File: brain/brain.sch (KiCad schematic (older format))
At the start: 0 parts

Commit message: footprint assignation
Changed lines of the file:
@@
 LIBS:contrib
 LIBS:valves
-LIBS:stm32
 LIBS:espitall
 LIBS:brain-cache
@@
 F11 "SLA_ALERT3_3v3" I R 2200 4700 60
 F12 "SLA_ALERT2_3v3" I R 2200 4600 60
+F13 "SLA_TX_3v3" I R 2200 3500 60
+F14 "SLA_RX_3v3" O R 2200 3600 60
 $EndSheet
 $Sheet
@@
 F1 "supply.sch" 60
 $EndSheet
+Wire Wire Line
+	2200 3600 4000 3600
+Wire Wire Line
+	4000 3500 2200 3500
 $EndSCHEMATC

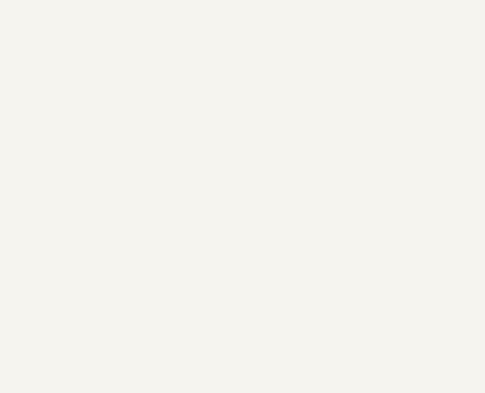
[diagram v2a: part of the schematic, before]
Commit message: add mounting holes
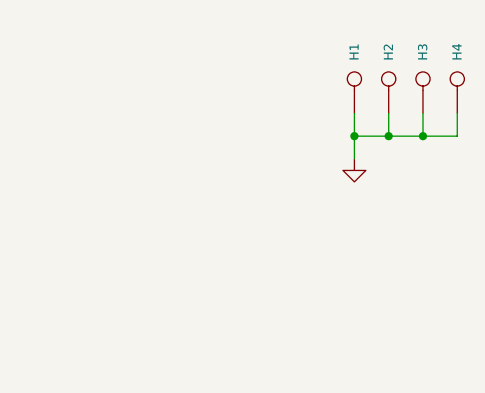
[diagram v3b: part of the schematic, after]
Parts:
- added H1, H2, H3, H4: CONN_1, Mounting_Holes:MountingHole_3-5mm, symbol CONN_1
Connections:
- new net GND: H1.1, H2.1, H3.1, H4.1
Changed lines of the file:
@@
 Wire Wire Line
 	4000 3500 2200 3500
+$Comp
+L CONN_1 H1
+U 1 1 5566D8A1
+P 10250 750
+F 0 "H1" H 10330 750 40  0000 L CNN
+F 1 "CONN_1" H 10250 805 30  0001 C CNN
+F 2 "Mounting_Holes:MountingHole_3-5mm" H 10250 750 60  0001 C CNN
+F 3 "" H 10250 750 60  0000 C CNN
+	1    10250 750
+	0    -1   -1   0
+$EndComp
+$Comp
+L CONN_1 H2
+U 1 1 5566FA8C
+P 10400 750
+F 0 "H2" H 10480 750 40  0000 L CNN
+F 1 "CONN_1" H 10400 805 30  0001 C CNN
+F 2 "Mounting_Holes:MountingHole_3-5mm" H 10400 750 60  0001 C CNN
+F 3 "" H 10400 750 60  0000 C CNN
+	1    10400 750
+	0    -1   -1   0
+$EndComp
+$Comp
+L CONN_1 H3
+U 1 1 5566FC24
+P 10550 750
+F 0 "H3" H 10630 750 40  0000 L CNN
+F 1 "CONN_1" H 10550 805 30  0001 C CNN
+F 2 "Mounting_Holes:MountingHole_3-5mm" H 10550 750 60  0001 C CNN
+F 3 "" H 10550 750 60  0000 C CNN
+	1    10550 750
+	0    -1   -1   0
+$EndComp
+$Comp
+L CONN_1 H4
+U 1 1 5566FDBE
+P 10700 750
+F 0 "H4" H 10780 750 40  0000 L CNN
+F 1 "CONN_1" H 10700 805 30  0001 C CNN
+F 2 "Mounting_Holes:MountingHole_3-5mm" H 10700 750 60  0001 C CNN
+F 3 "" H 10700 750 60  0000 C CNN
+	1    10700 750
+	0    -1   -1   0
+$EndComp
+$Comp
+L GND #PWR01
+U 1 1 55670260
+P 10250 1100
+F 0 "#PWR01" H 10250 1100 30  0001 C CNN
+F 1 "GND" H 10250 1030 30  0001 C CNN
+F 2 "" H 10250 1100 60  0000 C CNN
+F 3 "" H 10250 1100 60  0000 C CNN
+	1    10250 1100
+	1    0    0    -1
+$EndComp
+Wire Wire Line
+	10250 900  10250 1100
+Wire Wire Line
+	10250 1000 10700 1000
+Wire Wire Line
+	10700 1000 10700 900
+Connection ~ 10250 1000
+Wire Wire Line
+	10550 900  10550 1000
+Connection ~ 10550 1000
+Wire Wire Line
+	10400 900  10400 1000
+Connection ~ 10400 1000
 $EndSCHEMATC

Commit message: Brain 2018 layout
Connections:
- removed net GND: H1.1, H2.1, H3.1, H4.1
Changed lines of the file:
@@
 EESchema Schematic File Version 2
+LIBS:brain-rescue
 LIBS:power
 LIBS:device
@@
 LIBS:memory
 LIBS:xilinx
-LIBS:special
 LIBS:microcontrollers
 LIBS:dsp
@@
 $Descr A4 11693 8268
 encoding utf-8
-Sheet 1 8
+Sheet 1 9
 Title "Brain"
-Date ""
-Rev "2016"
-Comp "espitall"
-Comment1 "Board for eurobot 2016 (French edition)"
+Date "2017-05-28"
+Rev "2018"
+Comp "Cocobot"
+Comment1 "Board for eurobot 2018 (French edition)"
 Comment2 ""
 Comment3 ""
@@
 F11 "MOTL_PWM_3v3" I L 7200 5150 60
 F12 "MOTR_PWM_3v3" I L 7200 5350 60
-F13 "AX12_TX_3v3" I R 8600 4950 60
-F14 "AX12_RX_3v3" O R 8600 5050 60
-F15 "AX12_TX_5v" O R 8600 5150 60
-F16 "AX12_RX_5v" I R 8600 5250 60
-$EndSheet
-$Sheet
-S 7200 3800 1400 700
+$EndSheet
+$Sheet
+S 7200 3700 1350 300
 U 5563C415
 F0 "Servo" 60
 F1 "Servo.sch" 60
-F2 "I2C_SCL_3v3" I L 7200 4100 60
-F3 "I2C_SDA_3v3" B L 7200 4200 60
-F4 "AX12_TX_5v" I R 8600 4200 60
-F5 "AX12_RX_5v" O R 8600 4100 60
+F2 "I2C_SCL_3v3" I L 7200 3800 60
+F3 "I2C_SDA_3v3" B L 7200 3900 60
 $EndSheet
 $Sheet
@@
 F22 "MOTL_PWM_3v3" O R 6400 5150 60
 F23 "MOTR_PWM_3v3" O R 6400 5350 60
-F24 "I2C_SCL_3v3" O R 6400 4100 60
-F25 "I2C_SDA_3v3" B R 6400 4200 60
+F24 "I2C_SCL_3v3" O R 6400 3800 60
+F25 "I2C_SDA_3v3" B R 6400 3900 60
 F26 "IR_CH0_0_3v3" I L 4000 6350 60
 F27 "IR_CH1_0_3v3" I L 4000 6450 60
@@
 F35 "GPIO_SHIFT_OE_3v3" O R 6400 3000 60
 F36 "GPIO_SHIFT_STCP_3v3" O R 6400 2900 60
-F37 "AX12_TX_3v3" O R 6400 4700 60
-F38 "AX12_RX_3v3" I R 6400 4600 60
-F39 "US_CH0_E_3v3" I L 4000 5500 60
-F40 "US_CH1_E_3v3" I L 4000 5700 60
-F41 "US_CH3_E_3v3" I L 4000 6100 60
-F42 "US_CH2_E_3v3" I L 4000 5900 60
-F43 "US_CH1_T_3v3" O L 4000 5600 60
-F44 "US_CH0_T_3v3" O L 4000 5400 60
-F45 "US_CH3_T_3v3" O L 4000 6000 60
-F46 "US_CH2_T_3v3" O L 4000 5800 60
-F47 "GPIO0_3v3" B R 6400 1350 60
-F48 "GPIO1_3v3" B R 6400 1450 60
-F49 "GPIO2_3v3" B R 6400 1550 60
-F50 "GPIO3_3v3" B R 6400 1650 60
-F51 "GPIO4_3v3" B R 6400 1750 60
-F52 "GPIO5_3v3" B R 6400 1850 60
-F53 "GPIO6_3v3" B R 6400 1950 60
-F54 "GPIO7_3v3" B R 6400 2050 60
-F55 "GPIO8_3v3" B R 6400 2150 60
-F56 "GPIO9_3v3" B R 6400 2250 60
-F57 "GPIO10_3v3" B R 6400 2350 60
-F58 "GPIO11_3v3" B R 6400 2450 60
-F59 "STARTER_3v3" I R 6400 2550 60
-F60 "COLOR_3v3" I R 6400 2650 60
-F61 "SLA_TX_3v3" O L 4000 3500 60
-F62 "SLA_RX_3v3" I L 4000 3600 60
+F37 "US_CH0_E_3v3" I L 4000 5500 60
+F38 "US_CH1_E_3v3" I L 4000 5700 60
+F39 "US_CH3_E_3v3" I L 4000 6100 60
+F40 "US_CH2_E_3v3" I L 4000 5900 60
+F41 "US_CH1_T_3v3" O L 4000 5600 60
+F42 "US_CH0_T_3v3" O L 4000 5400 60
+F43 "US_CH3_T_3v3" O L 4000 6000 60
+F44 "US_CH2_T_3v3" O L 4000 5800 60
+F45 "GPIO0_3v3" B R 6400 1350 60
+F46 "GPIO1_3v3" B R 6400 1450 60
+F47 "GPIO2_3v3" B R 6400 1550 60
+F48 "GPIO3_3v3" B R 6400 1650 60
+F49 "GPIO4_3v3" B R 6400 1750 60
+F50 "GPIO5_3v3" B R 6400 1850 60
+F51 "GPIO6_3v3" B R 6400 1950 60
+F52 "GPIO7_3v3" B R 6400 2050 60
+F53 "GPIO8_3v3" B R 6400 2150 60
+F54 "GPIO9_3v3" B R 6400 2250 60
+F55 "GPIO10_3v3" B R 6400 2350 60
+F56 "GPIO11_3v3" B R 6400 2450 60
+F57 "STARTER_3v3" I R 6400 2550 60
+F58 "COLOR_3v3" I R 6400 2650 60
+F59 "SLA_TX_3v3" O L 4000 3500 60
+F60 "SLA_RX_3v3" I L 4000 3600 60
+F61 "DCM_PWM_0_3v3" O R 6400 4350 60
+F62 "DCM_PWM_1_3v3" O R 6400 4450 60
+F63 "DCM_DIR_0_3v3" O R 6400 4250 60
+F64 "DCM_DIR_1_3v3" O R 6400 4150 60
 $EndSheet
 Wire Wire Line
@@
 	6400 5050 7200 5050
 Wire Wire Line
-	7200 4950 6400 4950
+	6400 4950 7200 4950
 Wire Wire Line
 	7200 3300 3700 3300
@@
 	6400 1350 7200 1350
 Wire Wire Line
-	6400 4600 8900 4600
-Wire Wire Line
-	8900 4600 8900 5050
-Wire Wire Line
-	8900 5050 8600 5050
-Wire Wire Line
-	6400 4700 8800 4700
-Wire Wire Line
-	8800 4700 8800 4950
-Wire Wire Line
-	8800 4950 8600 4950
-Wire Wire Line
-	6400 4200 7200 4200
-Wire Wire Line
-	7200 4100 6400 4100
-Wire Wire Line
-	8600 5150 9000 5150
-Wire Wire Line
-	9000 5150 9000 4200
-Wire Wire Line
-	9000 4200 8600 4200
-Wire Wire Line
-	8600 5250 9100 5250
-Wire Wire Line
-	9100 5250 9100 4100
-Wire Wire Line
-	9100 4100 8600 4100
+	6400 3900 7200 3900
+Wire Wire Line
+	7200 3800 6400 3800
 $Sheet
 S 1200 1000 1000 800
@@
 	0    -1   -1   0
 $EndComp
-$Comp
-L GND #PWR1
-U 1 1 55670260
-P 10250 1100
-F 0 "#PWR1" H 10250 1100 30  0001 C CNN
-F 1 "GND" H 10250 1030 30  0001 C CNN
-F 2 "" H 10250 1100 60  0000 C CNN
-F 3 "" H 10250 1100 60  0000 C CNN
-	1    10250 1100
-	1    0    0    -1
-$EndComp
-Wire Wire Line
-	10250 900  10250 1100
-Wire Wire Line
-	10250 1000 10700 1000
-Wire Wire Line
-	10700 1000 10700 900
-Connection ~ 10250 1000
-Wire Wire Line
-	10550 900  10550 1000
-Connection ~ 10550 1000
-Wire Wire Line
-	10400 900  10400 1000
-Connection ~ 10400 1000
+$Sheet
+S 9050 4000 1900 800
+U 592BF177
+F0 "DC motor" 60
+F1 "DC_motor.sch" 60
+F2 "MOT_ENA_3v3" I L 9050 4550 60
+F3 "DCM0_DIR_3v3" I L 9050 4250 60
+F4 "DCM0_PWM_3v3" I L 9050 4350 60
+F5 "DCM1_PWM_3v3" I L 9050 4450 60
+F6 "DCM1_DIR_3v3" I L 9050 4150 60
+$EndSheet
+Wire Wire Line
+	9050 4550 6750 4550
+Wire Wire Line
+	6750 4550 6750 4950
+Connection ~ 6750 4950
+Wire Wire Line
+	9050 4450 6400 4450
+Wire Wire Line
+	6400 4350 9050 4350
+Wire Wire Line
+	6400 4150 9050 4150
+Wire Wire Line
+	9050 4250 6400 4250
 $EndSCHEMATC

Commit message: change shift register connector to match Cocoout and Cocoin
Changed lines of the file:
@@
 F0 "GPIO" 60
 F1 "gpio.sch" 60
-F2 "GPIO_SHIFT_STCP_3v3" I L 7200 2900 60
-F3 "GPIO_SHIFT_OE_3v3" I L 7200 3000 60
-F4 "SLA_SPI_SCK_3v3" I L 7200 3200 60
-F5 "SLA_SPI_MOSI_3v3" I L 7200 3300 60
-F6 "ANA_CH0_0_3v3" O L 7200 850 60
-F7 "ANA_CH1_0_3v3" O L 7200 950 60
-F8 "ANA_CH2_0_3v3" O L 7200 1050 60
-F9 "ANA_CH3_0_3v3" O L 7200 1150 60
-F10 "ANA_CH4_0_3v3" O L 7200 1250 60
-F11 "STARTER_3v3" O L 7200 2550 60
-F12 "COLOR_3v3" O L 7200 2650 60
-F13 "GPIO0_3v3" B L 7200 1350 60
-F14 "GPIO1_3v3" B L 7200 1450 60
-F15 "GPIO2_3v3" B L 7200 1550 60
-F16 "GPIO3_3v3" B L 7200 1650 60
-F17 "GPIO8_3v3" B L 7200 2150 60
-F18 "GPIO9_3v3" B L 7200 2250 60
-F19 "GPIO10_3v3" B L 7200 2350 60
-F20 "GPIO11_3v3" B L 7200 2450 60
-F21 "GPIO4_3v3" B L 7200 1750 60
-F22 "GPIO5_3v3" B L 7200 1850 60
-F23 "GPIO6_3v3" B L 7200 1950 60
-F24 "GPIO7_3v3" B L 7200 2050 60
+F2 "SLA_SPI_SCK_3v3" I L 7200 3200 60
+F3 "SLA_SPI_MOSI_3v3" I L 7200 3300 60
+F4 "ANA_CH0_0_3v3" O L 7200 850 60
+F5 "ANA_CH1_0_3v3" O L 7200 950 60
+F6 "ANA_CH2_0_3v3" O L 7200 1050 60
+F7 "ANA_CH3_0_3v3" O L 7200 1150 60
+F8 "ANA_CH4_0_3v3" O L 7200 1250 60
+F9 "STARTER_3v3" O L 7200 2550 60
+F10 "COLOR_3v3" O L 7200 2650 60
+F11 "GPIO0_3v3" B L 7200 1350 60
+F12 "GPIO1_3v3" B L 7200 1450 60
+F13 "GPIO2_3v3" B L 7200 1550 60
+F14 "GPIO3_3v3" B L 7200 1650 60
+F15 "GPIO8_3v3" B L 7200 2150 60
+F16 "GPIO9_3v3" B L 7200 2250 60
+F17 "GPIO10_3v3" B L 7200 2350 60
+F18 "GPIO11_3v3" B L 7200 2450 60
+F19 "GPIO4_3v3" B L 7200 1750 60
+F20 "GPIO5_3v3" B L 7200 1850 60
+F21 "GPIO6_3v3" B L 7200 1950 60
+F22 "GPIO7_3v3" B L 7200 2050 60
+F23 "GPIO_SHIFT_LOAD_3v3" I L 7200 2900 60
+F24 "GPIO_SHIFT_SET_3v3" I L 7200 3000 60
+F25 "SLA_SPI_MISO_3v3" I L 7200 3100 60
 $EndSheet
 $Sheet
@@
 F33 "ANA_CH1_0_3v3" I R 6400 950 60
 F34 "ANA_CH2_0_3v3" I R 6400 1050 60
-F35 "GPIO_SHIFT_OE_3v3" O R 6400 3000 60
-F36 "GPIO_SHIFT_STCP_3v3" O R 6400 2900 60
+F35 "GPIO_SHIFT_SET_3v3" O R 6400 3000 60
+F36 "GPIO_SHIFT_LOAD_3v3" O R 6400 2900 60
 F37 "US_CH0_E_3v3" I L 4000 5500 60
 F38 "US_CH1_E_3v3" I L 4000 5700 60
@@
 Wire Wire Line
 	9050 4250 6400 4250
+Wire Wire Line
+	7200 3100 3450 3100
+Wire Wire Line
+	3450 3100 3450 3800
+Connection ~ 3450 3800
 $EndSCHEMATC

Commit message: add 3d step files to brain
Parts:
- H1, H2, H3, H4: footprint Mounting_Holes:MountingHole_3-5mm -> Mounting_Holes:MountingHole_3.2mm_M3
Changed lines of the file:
@@
-EESchema Schematic File Version 2
+EESchema Schematic File Version 3
 LIBS:brain-rescue
-LIBS:power
-LIBS:device
-LIBS:transistors
-LIBS:conn
-LIBS:linear
-LIBS:regul
-LIBS:74xx
-LIBS:cmos4000
-LIBS:adc-dac
-LIBS:memory
-LIBS:xilinx
-LIBS:microcontrollers
-LIBS:dsp
-LIBS:microchip
-LIBS:analog_switches
-LIBS:motorola
-LIBS:texas
-LIBS:intel
-LIBS:audio
-LIBS:interface
-LIBS:digital-audio
-LIBS:philips
-LIBS:display
-LIBS:cypress
-LIBS:siliconi
-LIBS:opto
-LIBS:atmel
-LIBS:contrib
-LIBS:valves
 LIBS:espitall
 LIBS:brain-cache
-EELAYER 25 0
+EELAYER 26 0
 EELAYER END
 $Descr A4 11693 8268
@@
 F 0 "H1" H 10330 750 40  0000 L CNN
 F 1 "CONN_1" H 10250 805 30  0001 C CNN
-F 2 "Mounting_Holes:MountingHole_3-5mm" H 10250 750 60  0001 C CNN
+F 2 "Mounting_Holes:MountingHole_3.2mm_M3" H 10250 750 60  0001 C CNN
 F 3 "" H 10250 750 60  0000 C CNN
 	1    10250 750
@@
 F 0 "H2" H 10480 750 40  0000 L CNN
 F 1 "CONN_1" H 10400 805 30  0001 C CNN
-F 2 "Mounting_Holes:MountingHole_3-5mm" H 10400 750 60  0001 C CNN
+F 2 "Mounting_Holes:MountingHole_3.2mm_M3" H 10400 750 60  0001 C CNN
 F 3 "" H 10400 750 60  0000 C CNN
 	1    10400 750
@@
 F 0 "H3" H 10630 750 40  0000 L CNN
 F 1 "CONN_1" H 10550 805 30  0001 C CNN
-F 2 "Mounting_Holes:MountingHole_3-5mm" H 10550 750 60  0001 C CNN
+F 2 "Mounting_Holes:MountingHole_3.2mm_M3" H 10550 750 60  0001 C CNN
 F 3 "" H 10550 750 60  0000 C CNN
 	1    10550 750
@@
 F 0 "H4" H 10780 750 40  0000 L CNN
 F 1 "CONN_1" H 10700 805 30  0001 C CNN
-F 2 "Mounting_Holes:MountingHole_3-5mm" H 10700 750 60  0001 C CNN
+F 2 "Mounting_Holes:MountingHole_3.2mm_M3" H 10700 750 60  0001 C CNN
 F 3 "" H 10700 750 60  0000 C CNN
 	1    10700 750

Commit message: add module add footprint SPSGRF-868 for future com board
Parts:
- H1, H2, H3, H4: symbol CONN_1 -> brain-rescue:CONN_1-RESCUE-brain
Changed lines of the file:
@@
-EESchema Schematic File Version 3
-LIBS:brain-rescue
-LIBS:espitall
+EESchema Schematic File Version 4
 LIBS:brain-cache
 EELAYER 26 0
@@
 	2200 4000 4000 4000
 Wire Wire Line
-	2200 3900 4000 3900
-Wire Wire Line
-	2200 3800 4000 3800
-Wire Wire Line
-	2200 3700 4000 3700
+	2200 3900 3700 3900
+Wire Wire Line
+	2200 3800 3450 3800
+Wire Wire Line
+	2200 3700 3600 3700
 Wire Wire Line
 	2200 4500 4000 4500
@@
 	6400 5050 7200 5050
 Wire Wire Line
-	6400 4950 7200 4950
+	6400 4950 6750 4950
 Wire Wire Line
 	7200 3300 3700 3300
@@
 	4000 3500 2200 3500
 $Comp
-L CONN_1 H1
+L brain-rescue:CONN_1-RESCUE-brain H1
 U 1 1 5566D8A1
 P 10250 750
@@
 $EndComp
 $Comp
-L CONN_1 H2
+L brain-rescue:CONN_1-RESCUE-brain H2
 U 1 1 5566FA8C
 P 10400 750
@@
 $EndComp
 $Comp
-L CONN_1 H3
+L brain-rescue:CONN_1-RESCUE-brain H3
 U 1 1 5566FC24
 P 10550 750
@@
 $EndComp
 $Comp
-L CONN_1 H4
+L brain-rescue:CONN_1-RESCUE-brain H4
 U 1 1 5566FDBE
 P 10700 750
@@
 	3450 3100 3450 3800
 Connection ~ 3450 3800
+Wire Wire Line
+	3700 3900 4000 3900
+Wire Wire Line
+	3600 3700 4000 3700
+Wire Wire Line
+	6750 4950 7200 4950
+Wire Wire Line
+	3450 3800 4000 3800
 $EndSCHEMATC
